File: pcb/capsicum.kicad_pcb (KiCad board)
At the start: 2 copper layers, 70 x 55 mm, 79 parts, among them J2 Screw terminal, J3 USB-C 16+8 USB 2.0, Q1 NS2101P, Q2 BC817, SW1 SW_SPDT, SW3 SW_SPDT, U1 ESP32-C3-WROOM-02, U2 TQ33E-1, U3 AP2112K, U4 MCP73831

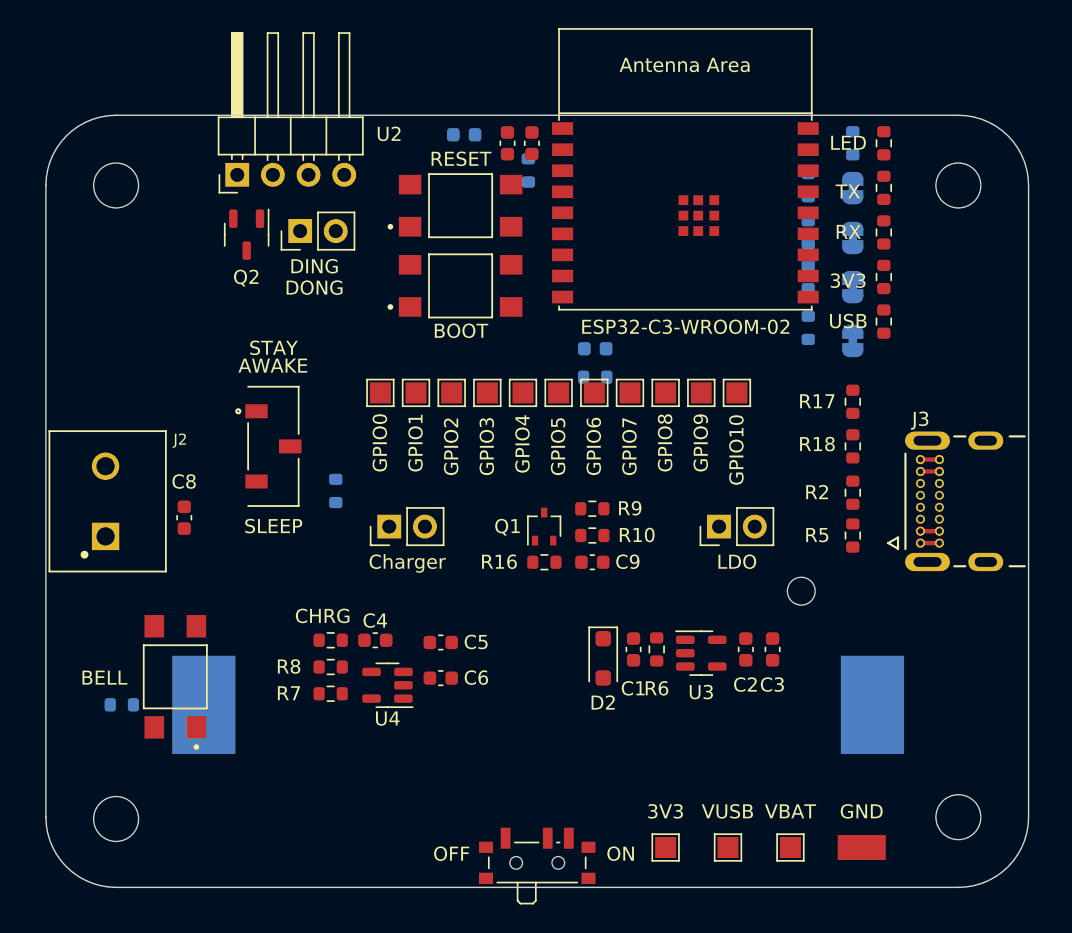
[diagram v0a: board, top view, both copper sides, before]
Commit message: refactor: change board shape to make way for teeth and groove
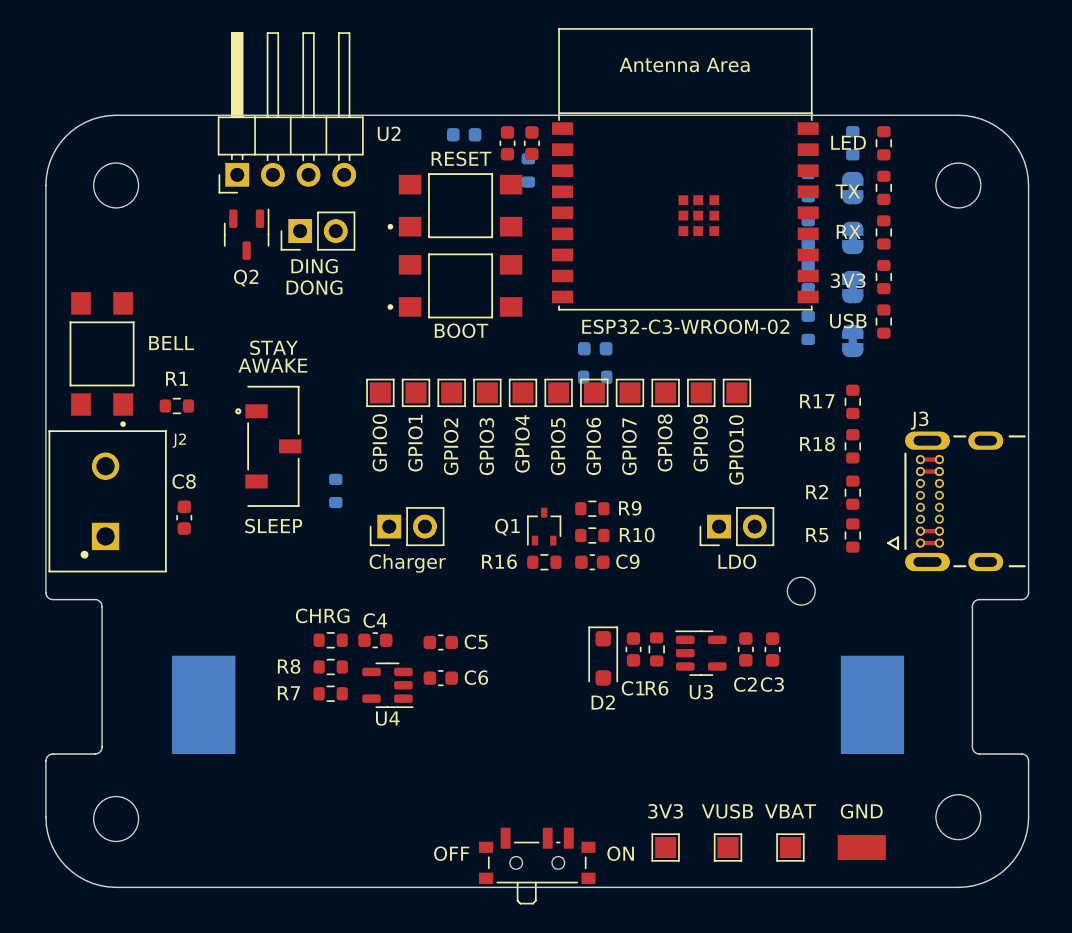
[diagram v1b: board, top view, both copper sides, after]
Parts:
- R1: moved to F.Cu
- moved S1 23.6 mm to (104.0, 102.0)
- moved R1 21.6 mm to (109.3, 105.7), turned to 0 degrees
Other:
- outline, holes or cut-outs redrawn
- board text added: "teeth and groove"

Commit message: refactor: move LEDs, USB-C and Screw terminal connectors in PCB layout
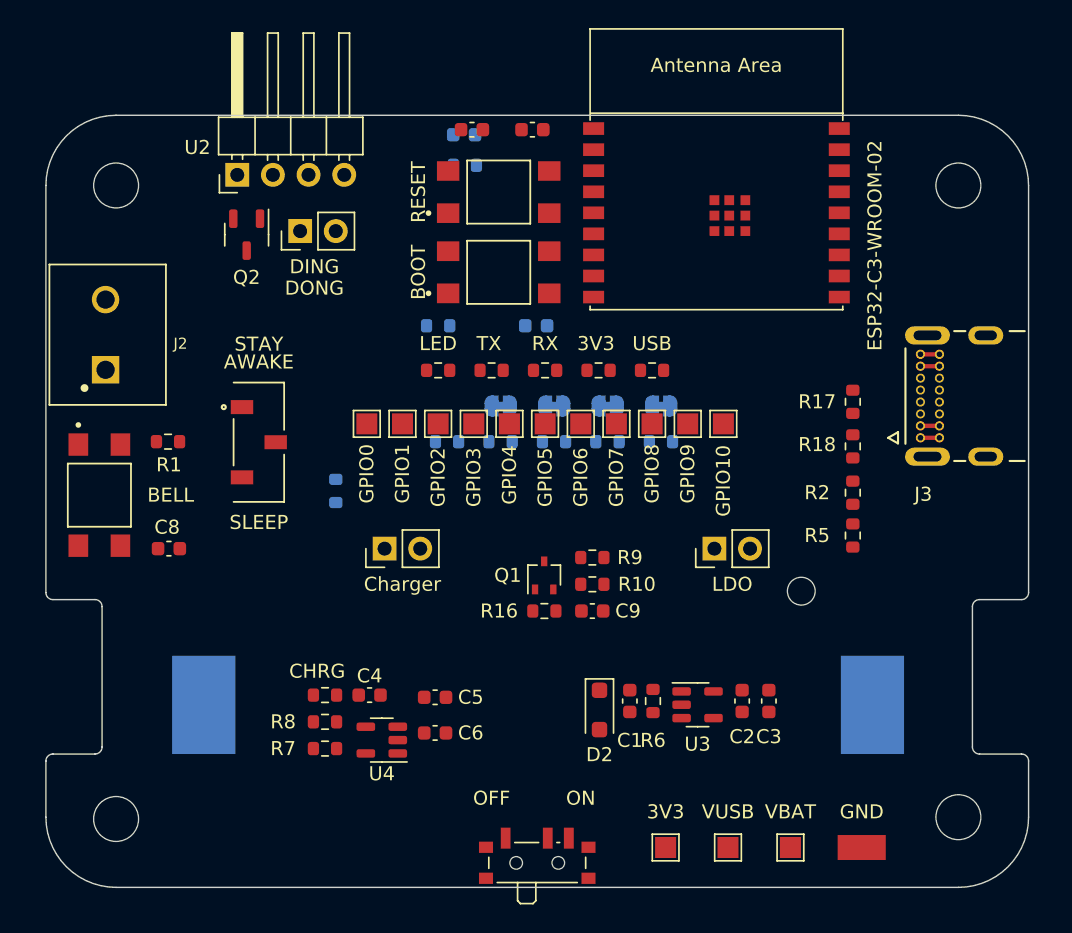
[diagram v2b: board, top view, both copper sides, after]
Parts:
- moved R3 35.9 mm to (128.6, 108.2), turned to 180 degrees
- moved D1 35.6 mm to (127.9, 103.2), turned to 180 degrees
- moved ? 35.0 mm to (109.1, 112.8)
- moved D4 30.8 mm to (131.8, 103.2), turned to 0 degrees
- moved JP6 29.5 mm to (132.4, 105.7), turned to 180 degrees
- moved R11 28.5 mm to (132.4, 108.2), turned to 0 degrees
- moved D5 26.1 mm to (135.6, 103.2), turned to 180 degrees
- moved JP7 24.4 mm to (136.2, 105.7), turned to 0 degrees
- moved R12 23.5 mm to (136.2, 108.2), turned to 180 degrees
- moved D7 21.4 mm to (139.4, 103.2), turned to 180 degrees
- moved JP5 19.4 mm to (140.0, 105.7), turned to 0 degrees
- moved R15 18.5 mm to (140.0, 108.2), turned to 180 degrees
- moved D6 16.9 mm to (143.2, 103.2), turned to 0 degrees
- moved JP4 14.4 mm to (143.8, 105.7), turned to 180 degrees
- moved R14 13.3 mm to (143.8, 108.2), turned to 0 degrees
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
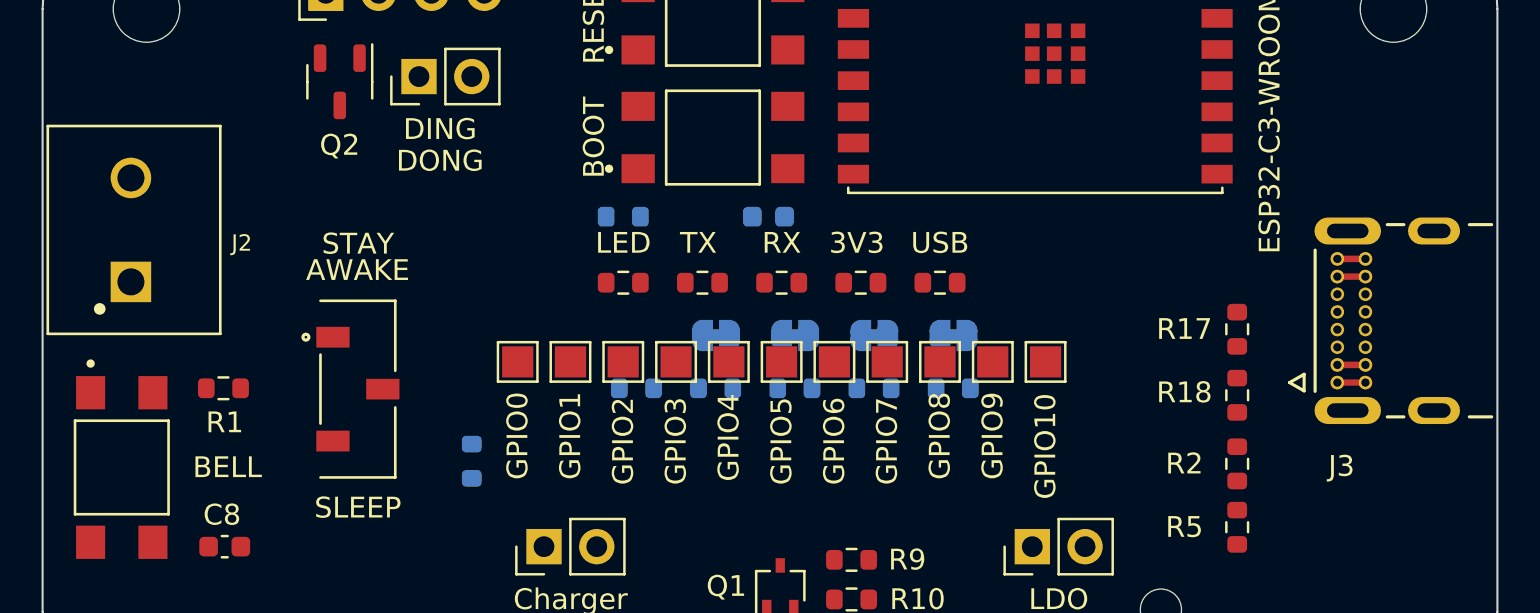
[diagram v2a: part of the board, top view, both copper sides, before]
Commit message: refactor: move screw terminal and USB-C connectors
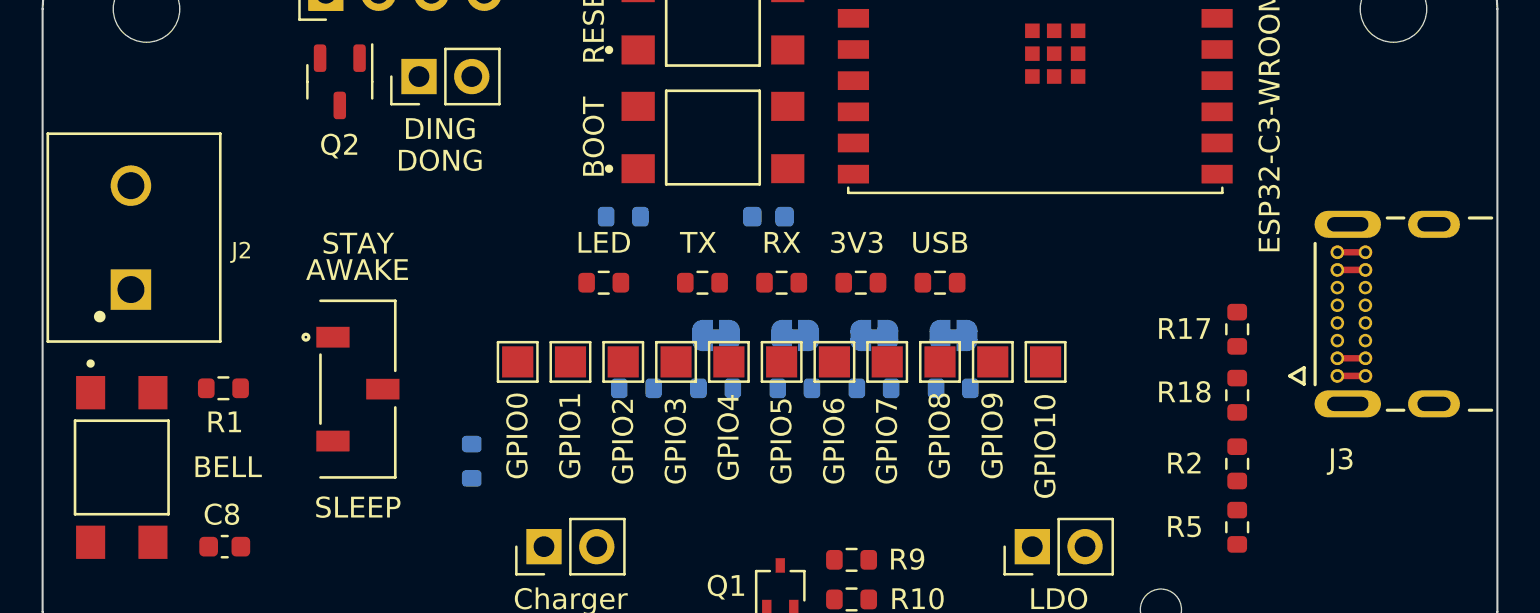
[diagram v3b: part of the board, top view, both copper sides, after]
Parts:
- moved D1 0.94 mm to (127.0, 103.2)
- moved J2 0.37 mm to (104.2, 101.0)
- moved J3 0.32 mm to (169.9, 104.7)
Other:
- board text added: "pcb_width"
- board text added: "screw_terminal_y"
- board text added: "usbc_y"

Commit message: refactor: move LED slot
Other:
- board text added: "led_row_length"
- board text added: "led_row_width"
- board text added: "led_row_x"
- board text added: "led_row_y"
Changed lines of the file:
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@@
   (title_block
     (title "Capsicum")
-    (date "2024-01-26")
+    (date "2024-01-30")
     (comment 1 "Authored by: Sayanee Basu")
     (comment 2 "Project website: https://hutscape.com/capsicum")
@@
     (effects (font (size 1 1) (thickness 0.15)) (justify left bottom))
   )
+  (gr_text "led_row_y" (at 58.5 125.5 90) (layer "Dwgs.User")
+    (effects (font (size 1 1) (thickness 0.15)) (justify left bottom))
+  )
+  (gr_text "led_row_length" (at 129.5 174) (layer "Dwgs.User")
+    (effects (font (size 1 1) (thickness 0.15)) (justify left bottom))
+  )
+  (gr_text "led_row_width" (at 55.5 108.5 90) (layer "Dwgs.User")
+    (effects (font (size 1 1) (thickness 0.15)) (justify left bottom))
+  )
   (gr_text "teeth\nand \ngroove" (at 97.5 127) (layer "Dwgs.User")
     (effects (font (size 1 1) (thickness 0.15)) (justify left bottom))
@@
     (effects (font (size 1 1) (thickness 0.15)) (justify left bottom))
   )
+  (gr_text "led_row_x" (at 108.5 170.5) (layer "Dwgs.User")
+    (effects (font (size 1 1) (thickness 0.15)) (justify left bottom))
+  )
   (dimension (type aligned) (layer "Dwgs.User")
     (pts (xy 100 130) (xy 100 120))
@@
   )
   (dimension (type aligned) (layer "Dwgs.User")
-    (pts (xy 179 101.5) (xy 179 140))
-    (height -4.5)
-    (gr_text "38.5000 mm" (at 182.35 120.75 90) (layer "Dwgs.User")
-      (effects (font (size 1 1) (thickness 0.15)))
-    )
-    (format (prefix "") (suffix "") (units 3) (units_format 1) (precision 4))
-    (style (thickness 0.15) (arrow_length 1.27) (text_position_mode 0) (extension_height 0.58642) (extension_offset 0.5) keep_text_aligned)
-  )
-  (dimension (type aligned) (layer "Dwgs.User")
     (pts (xy 160.5 84.5) (xy 170.5 84.5))
     (height -4.5)
@@
   )
   (dimension (type aligned) (layer "Dwgs.User")
-    (pts (xy 162.5 85) (xy 162.5 101.5))
-    (height -13.5)
-    (gr_text "16.5000 mm" (at 174.85 93.25 90) (layer "Dwgs.User")
-      (effects (font (size 1 1) (thickness 0.15)))
-    )
-    (format (prefix "") (suffix "") (units 3) (units_format 1) (precision 4))
-    (style (thickness 0.15) (arrow_length 1.27) (text_position_mode 0) (extension_height 0.58642) (extension_offset 0.5) keep_text_aligned)
-  )
-  (dimension (type aligned) (layer "Dwgs.User")
-    (pts (xy 100 104.5) (xy 125.5 104.5))
-    (height 64.5)
-    (gr_text "25.5000 mm" (at 112.75 167.85) (layer "Dwgs.User")
-      (effects (font (size 1 1) (thickness 0.15)))
-    )
-    (format (prefix "") (suffix "") (units 3) (units_format 1) (precision 4))
-    (style (thickness 0.15) (arrow_length 1.27) (text_position_mode 0) (extension_height 0.58642) (extension_offset 0.5) keep_text_aligned)
-  )
-  (dimension (type aligned) (layer "Dwgs.User")
     (pts (xy 100 140) (xy 100 130))
     (height -14)
@@
   )
   (dimension (type aligned) (layer "Dwgs.User")
+    (pts (xy 124.5 104.5) (xy 124.5 140))
+    (height 63.5)
+    (gr_text "35.5000 mm" (at 59.85 122.25 90) (layer "Dwgs.User")
+      (effects (font (size 1 1) (thickness 0.15)))
+    )
+    (format (prefix "") (suffix "") (units 3) (units_format 1) (precision 4))
+    (style (thickness 0.15) (arrow_length 1.27) (text_position_mode 0) (extension_height 0.58642) (extension_offset 0.5) keep_text_aligned)
+  )
+  (dimension (type aligned) (layer "Dwgs.User")
     (pts (xy 100 145) (xy 170 145))
     (height 0)
@@
   )
   (dimension (type aligned) (layer "Dwgs.User")
+    (pts (xy 125 104.5) (xy 125 102))
+    (height -67)
+    (gr_text "2.5000 mm" (at 56.85 103.25 90) (layer "Dwgs.User")
+      (effects (font (size 1 1) (thickness 0.15)))
+    )
+    (format (prefix "") (suffix "") (units 3) (units_format 1) (precision 4))
+    (style (thickness 0.15) (arrow_length 1.27) (text_position_mode 0) (extension_height 0.58642) (extension_offset 0.5) keep_text_aligned)
+  )
+  (dimension (type aligned) (layer "Dwgs.User")
+    (pts (xy 124.5 104.5) (xy 100 104.5))
+    (height -64.5)
+    (gr_text "24.5000 mm" (at 112.25 167.85) (layer "Dwgs.User")
+      (effects (font (size 1 1) (thickness 0.15)))
+    )
+    (format (prefix "") (suffix "") (units 3) (units_format 1) (precision 4))
+    (style (thickness 0.15) (arrow_length 1.27) (text_position_mode 0) (extension_height 0.58642) (extension_offset 0.5) keep_text_aligned)
+  )
+  (dimension (type aligned) (layer "Dwgs.User")
     (pts (xy 105 90) (xy 105 85))
     (height -16.5)
@@
       (effects (font (size 1 1) (thickness 0.15)))
     )
+    (format (prefix "") (suffix "") (units 3) (units_format 1) (precision 4))
+    (style (thickness 0.15) (arrow_length 1.27) (text_position_mode 0) (extension_height 0.58642) (extension_offset 0.5) keep_text_aligned)
+  )
+  (dimension (type aligned) (layer "Dwgs.User")
+    (pts (xy 124.5 104.5) (xy 145.5 104.5))
+    (height 72)
+    (gr_text "21.0000 mm" (at 135 175.35) (layer "Dwgs.User")
+      (effects (font (size 1 1) (thickness 0.15)))
+    )

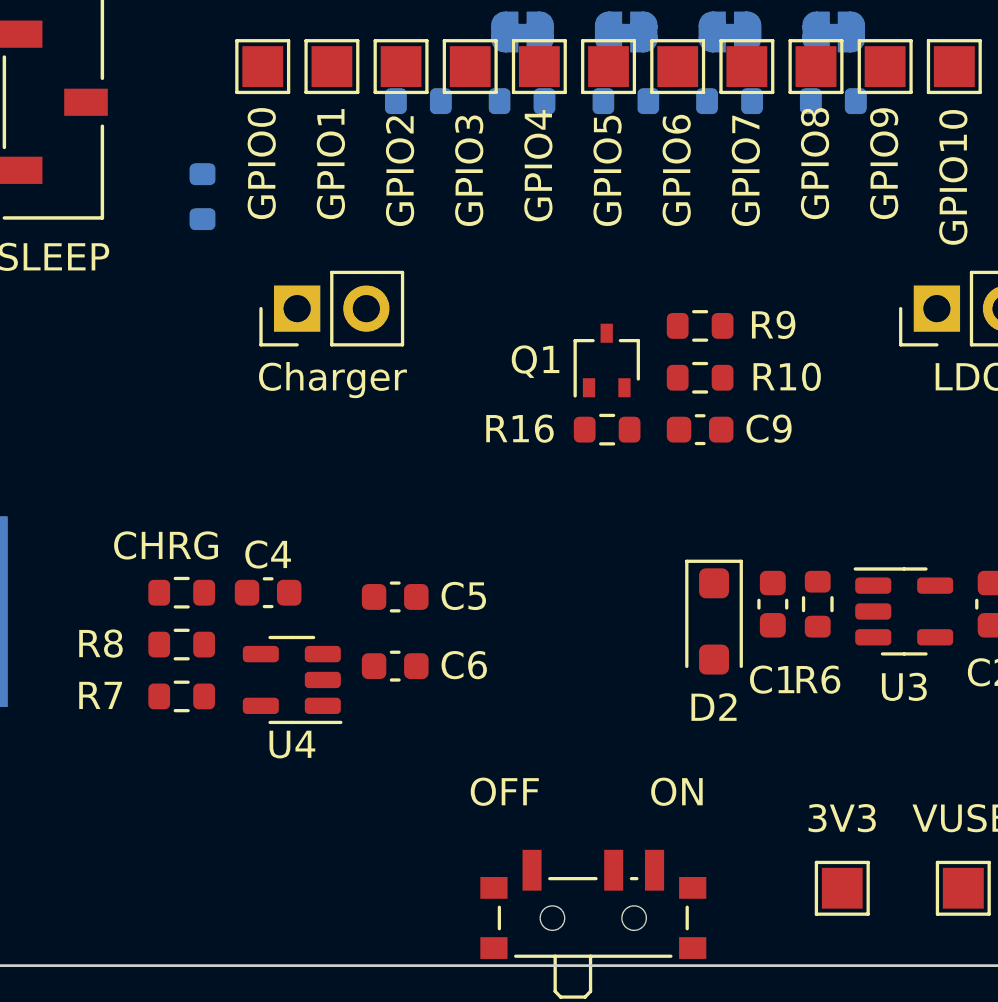
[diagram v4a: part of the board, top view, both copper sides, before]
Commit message: refactor: update all measurement labels in KiCAD with labels from FreeCAD
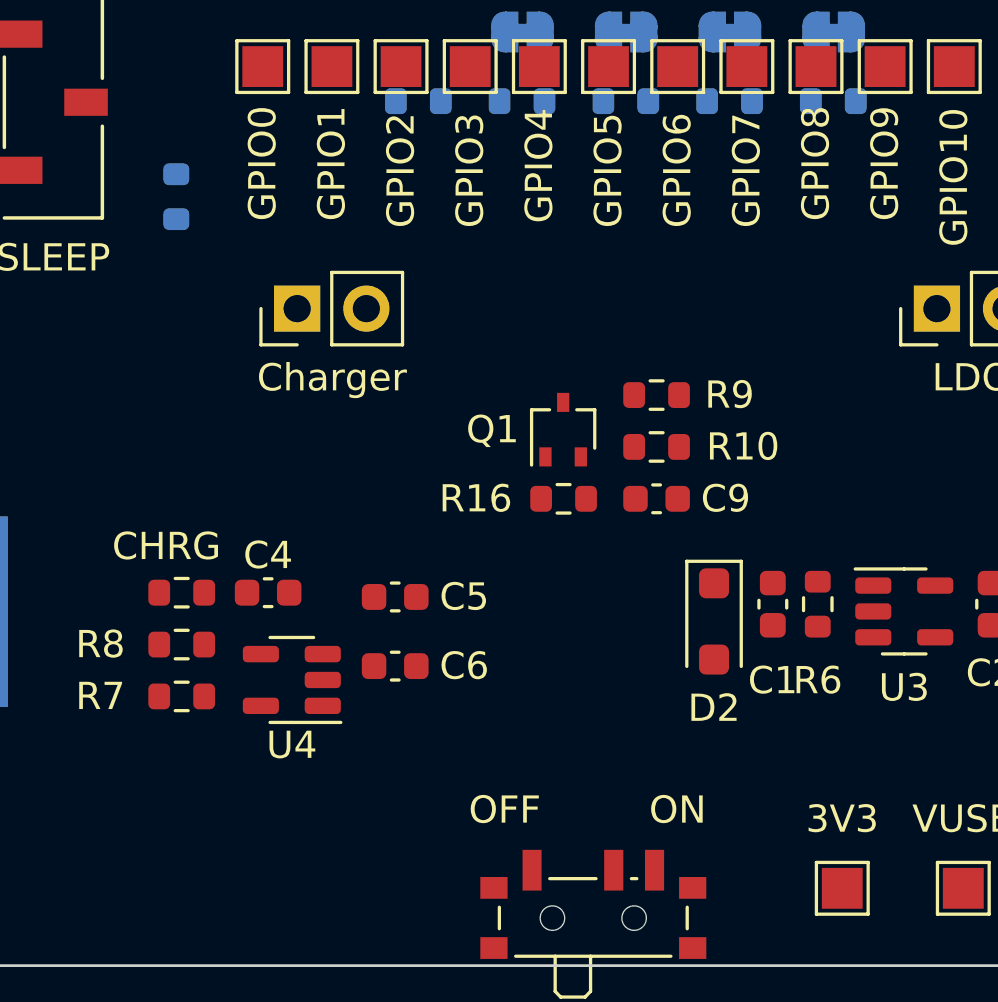
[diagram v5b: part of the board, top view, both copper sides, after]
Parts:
- moved C9 3.00 mm to (137.3, 122.9)
- moved R10 3.00 mm to (137.3, 121.0)
- moved R9 3.00 mm to (137.3, 119.0)
- moved R16 3.00 mm to (133.9, 122.9)
- moved Q1 3.00 mm to (133.9, 120.3)
- moved R4 0.97 mm to (119.7, 111.8)
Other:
- board text added: "battery_holder_length"
- board text added: "battery_holder_mid_y"
- board text added: "pcb_length"
- board text added: "screw_terminal_length"
- board text added: "screw_x_y"
- board text added: "switch_on_off_length"
- board text added: "switch_on_off_x"
- board text added: "teeth_length"
- board text added: "teeth_placement_x"
- board text added: "usb_c_width"
